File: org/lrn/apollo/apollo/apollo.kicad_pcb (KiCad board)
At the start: 2 copper layers, 28 parts, among them J1 Conn_01x01_Male, J2 Conn_01x01_Male, J3 Conn_01x01_Male, J4 Conn_01x01_Male, Q1 PN2222A, Q2 PN2222A, Q3 PN2222A, Q4 PN2222A, U1 74HC595, U2 5461AS-1

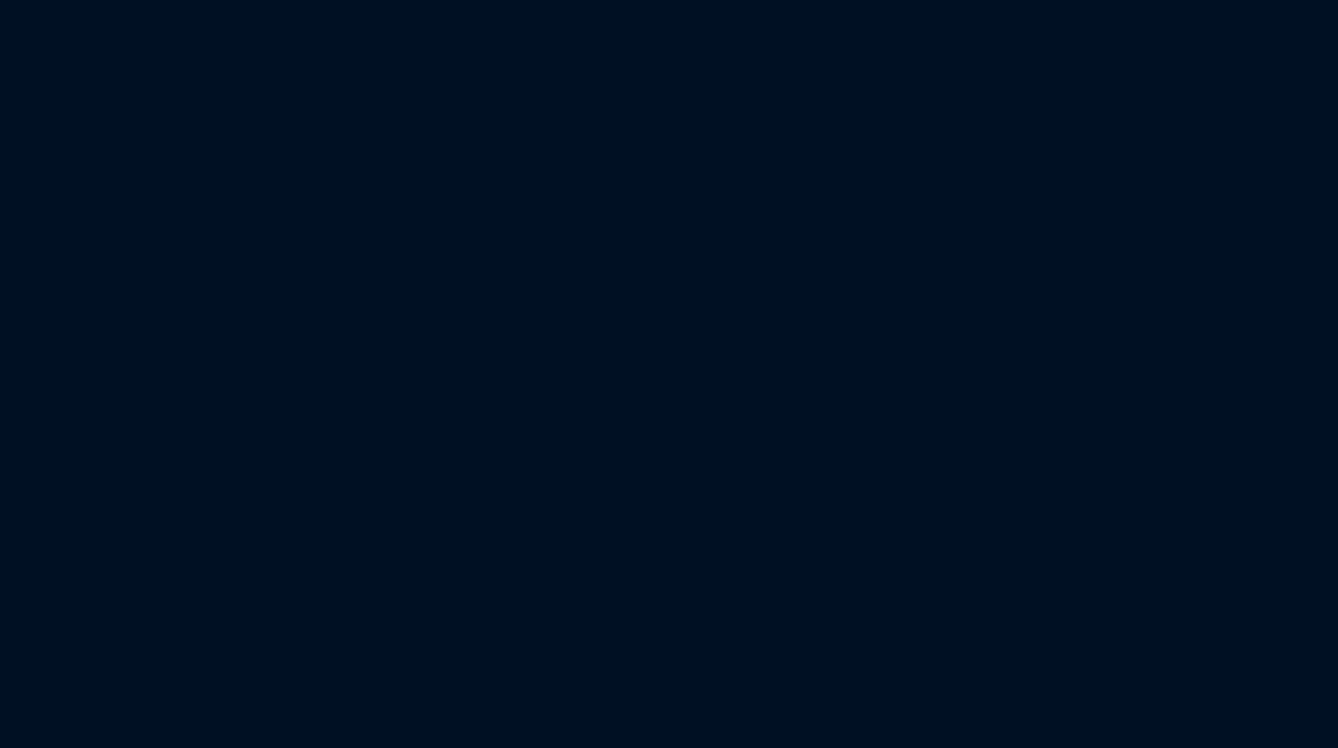
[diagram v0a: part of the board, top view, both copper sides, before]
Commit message: apollo: schematic for keyb shift register
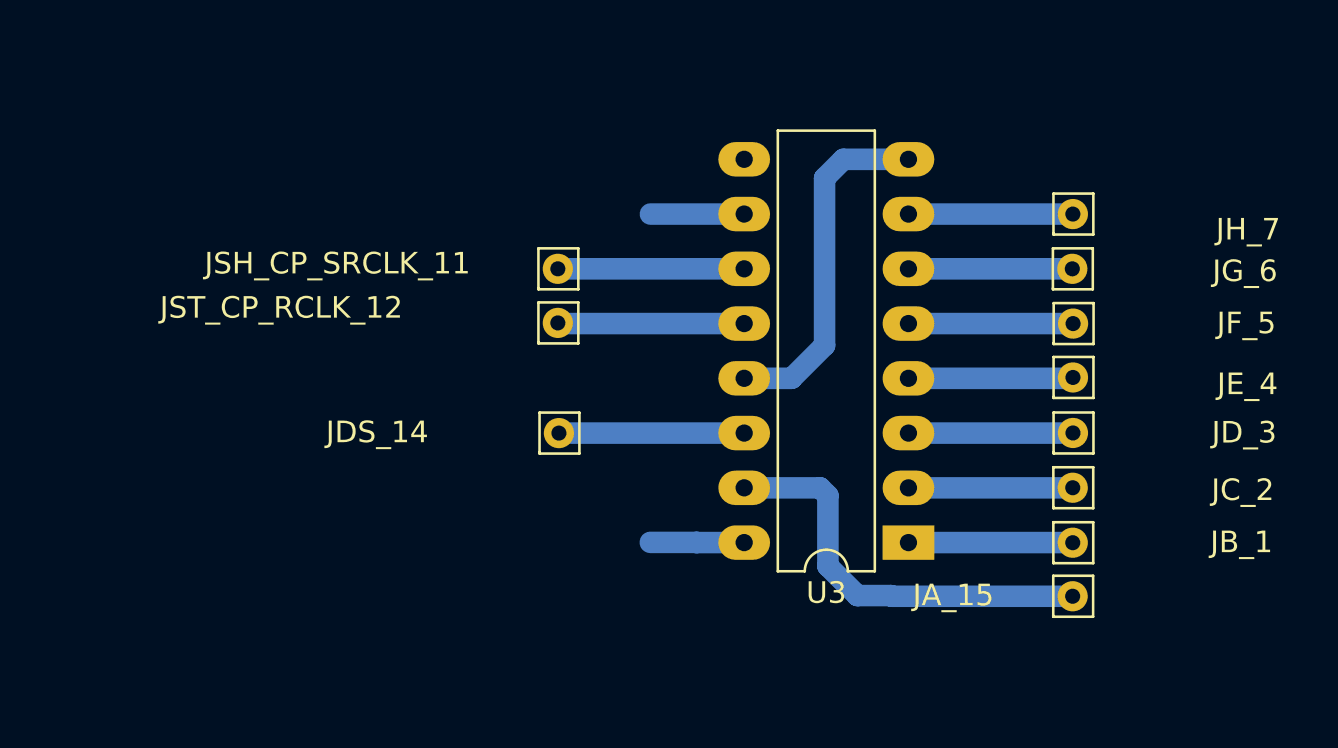
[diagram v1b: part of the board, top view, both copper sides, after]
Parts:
- added JA_15: Conn_01x01_Male, Connector_Pin:Pin_D0.7mm_L6.5mm_W1.8mm_FlatFork, F.Cu at (153.2, 95.3)
- added JB_1: Conn_01x01_Male, Connector_Pin:Pin_D0.7mm_L6.5mm_W1.8mm_FlatFork, F.Cu at (153.2, 92.8)
- added JC_2: Conn_01x01_Male, Connector_Pin:Pin_D0.7mm_L6.5mm_W1.8mm_FlatFork, F.Cu at (153.2, 90.3)
- added JDS_14: Conn_01x01_Male, Connector_Pin:Pin_D0.7mm_L6.5mm_W1.8mm_FlatFork, F.Cu at (129.4, 87.7)
- added JD_3: Conn_01x01_Male, Connector_Pin:Pin_D0.7mm_L6.5mm_W1.8mm_FlatFork, F.Cu at (153.2, 87.7)
- added JE_4: Conn_01x01_Male, Connector_Pin:Pin_D0.7mm_L6.5mm_W1.8mm_FlatFork, F.Cu at (153.2, 85.2)
- added JF_5: Conn_01x01_Male, Connector_Pin:Pin_D0.7mm_L6.5mm_W1.8mm_FlatFork, F.Cu at (153.2, 82.7)
- added JG_6: Conn_01x01_Male, Connector_Pin:Pin_D0.7mm_L6.5mm_W1.8mm_FlatFork, F.Cu at (153.2, 80.1)
- added JH_7: Conn_01x01_Male, Connector_Pin:Pin_D0.7mm_L6.5mm_W1.8mm_FlatFork, F.Cu at (153.2, 77.6)
- added JSH_CP_SRCLK_11: Conn_01x01_Male, Connector_Pin:Pin_D0.7mm_L6.5mm_W1.8mm_FlatFork, F.Cu at (129.3, 80.1)
- added JST_CP_RCLK_12: Conn_01x01_Male, Connector_Pin:Pin_D0.7mm_L6.5mm_W1.8mm_FlatFork, F.Cu at (129.3, 82.6)
- added U3: 74HC595, Package_DIP:DIP-16_W7.62mm_LongPads, F.Cu at (145.6, 92.8)
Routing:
- net Net-(JA_15-Pad1): track 0.00 -> 19.2 mm
- net GND: track 143.5 -> 159.8 mm
- net VCC: track 27.1 -> 36.1 mm
- net Net-(JST_CP_RCLK_12-Pad1): track 0.00 -> 8.66 mm
- net Net-(JSH_CP_SRCLK_11-Pad1): track 0.00 -> 8.64 mm
- net Net-(JDS_14-Pad1): track 0.00 -> 8.59 mm
- net Net-(JE_4-Pad1): track 0.00 -> 7.65 mm
- net Net-(JF_5-Pad1): track 0.00 -> 7.64 mm
- net Net-(JD_3-Pad1): track 0.00 -> 7.63 mm
- net Net-(JH_7-Pad1): track 0.00 -> 7.63 mm
- net Net-(JB_1-Pad1): track 0.00 -> 7.62 mm
- net Net-(JC_2-Pad1): track 0.00 -> 7.62 mm
- net Net-(JG_6-Pad1): track 0.00 -> 7.60 mm

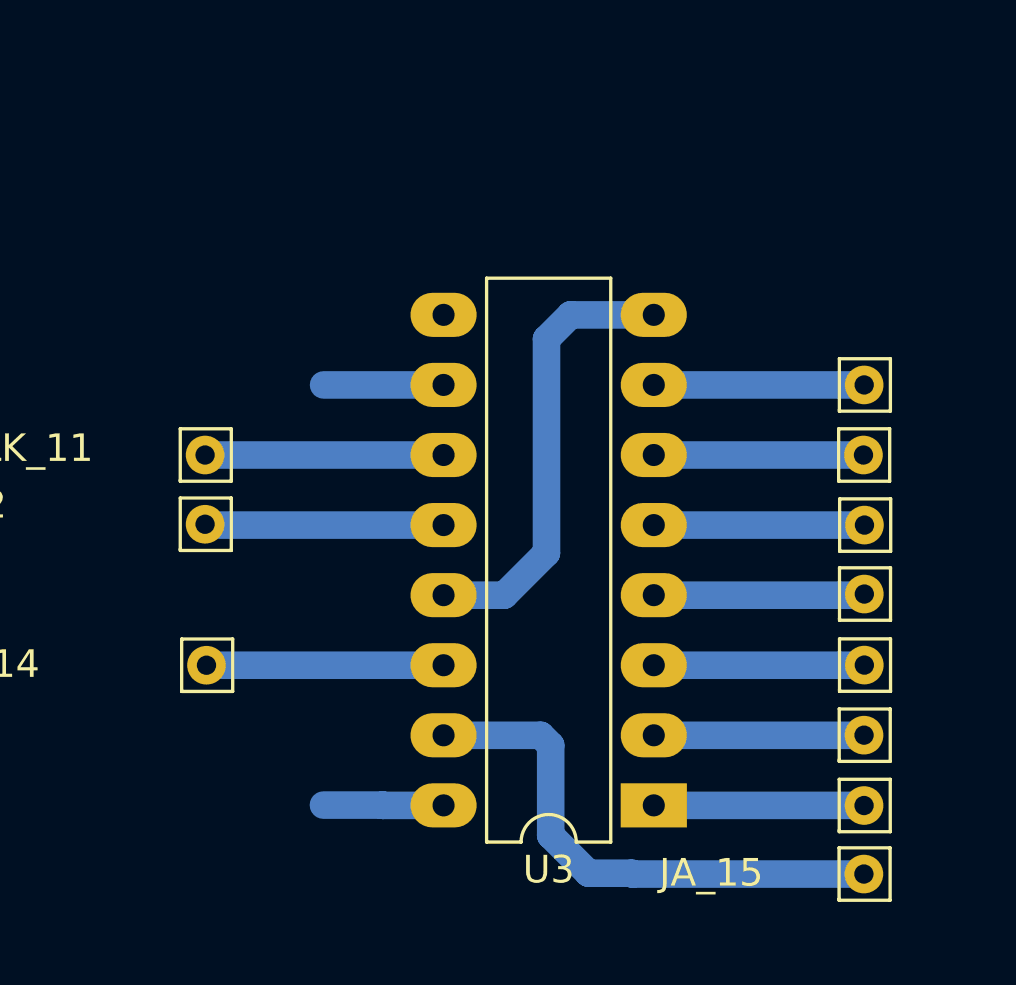
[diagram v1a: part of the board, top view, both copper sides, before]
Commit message: apollo: keyb driver: additional track-vias
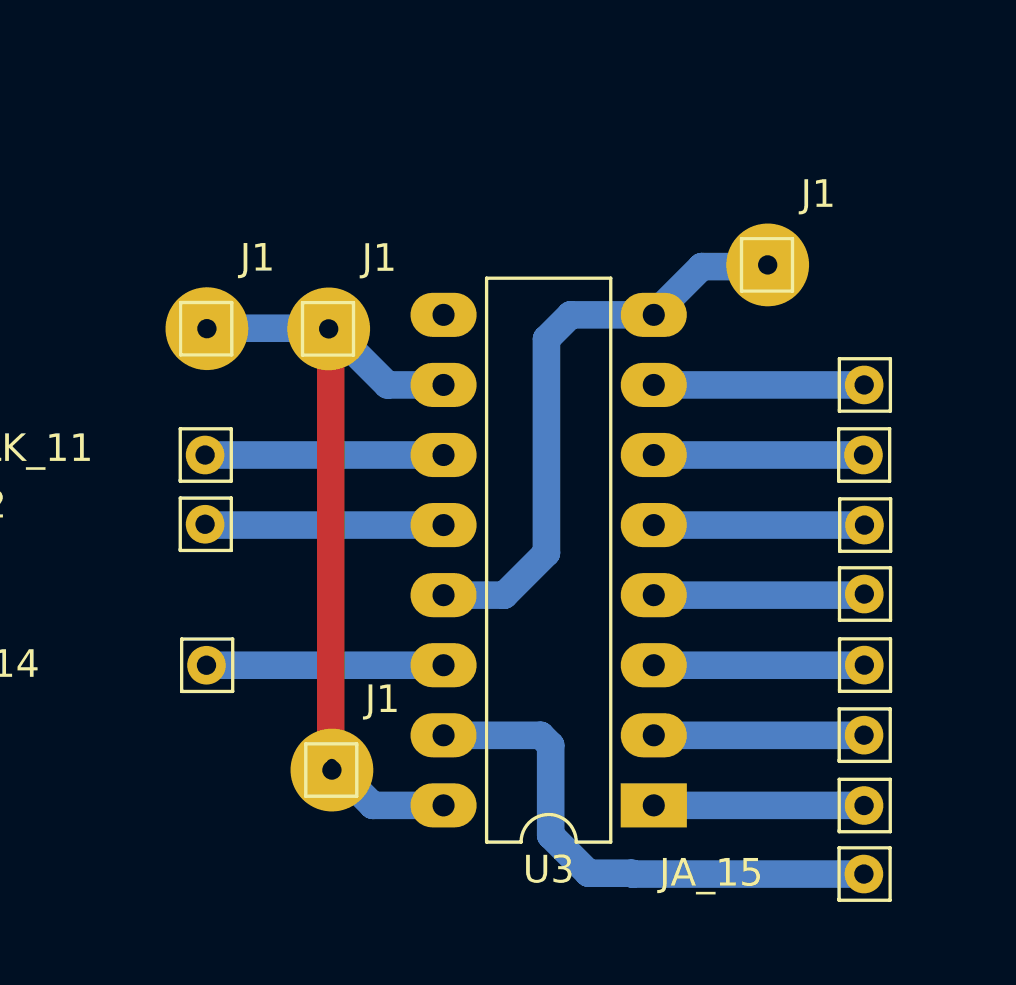
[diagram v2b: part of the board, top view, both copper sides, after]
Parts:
- added J1: Conn_01x01_Male, Connector_Pin:Pin_D0.7mm_L6.5mm_W1.8mm_FlatFork, F.Cu at (133.8, 75.6)
- added J1: Conn_01x01_Male, Connector_Pin:Pin_D0.7mm_L6.5mm_W1.8mm_FlatFork, F.Cu at (133.9, 91.5)
- added J1: Conn_01x01_Male, Connector_Pin:Pin_D0.7mm_L6.5mm_W1.8mm_FlatFork, F.Cu at (129.4, 75.5)
- added J1: Conn_01x01_Male, Connector_Pin:Pin_D0.7mm_L6.5mm_W1.8mm_FlatFork, F.Cu at (149.7, 73.2)
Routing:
- net VCC: track 36.1 -> 56.8 mm, vias 0 -> 2
- net GND: track 159.8 -> 164.7 mm

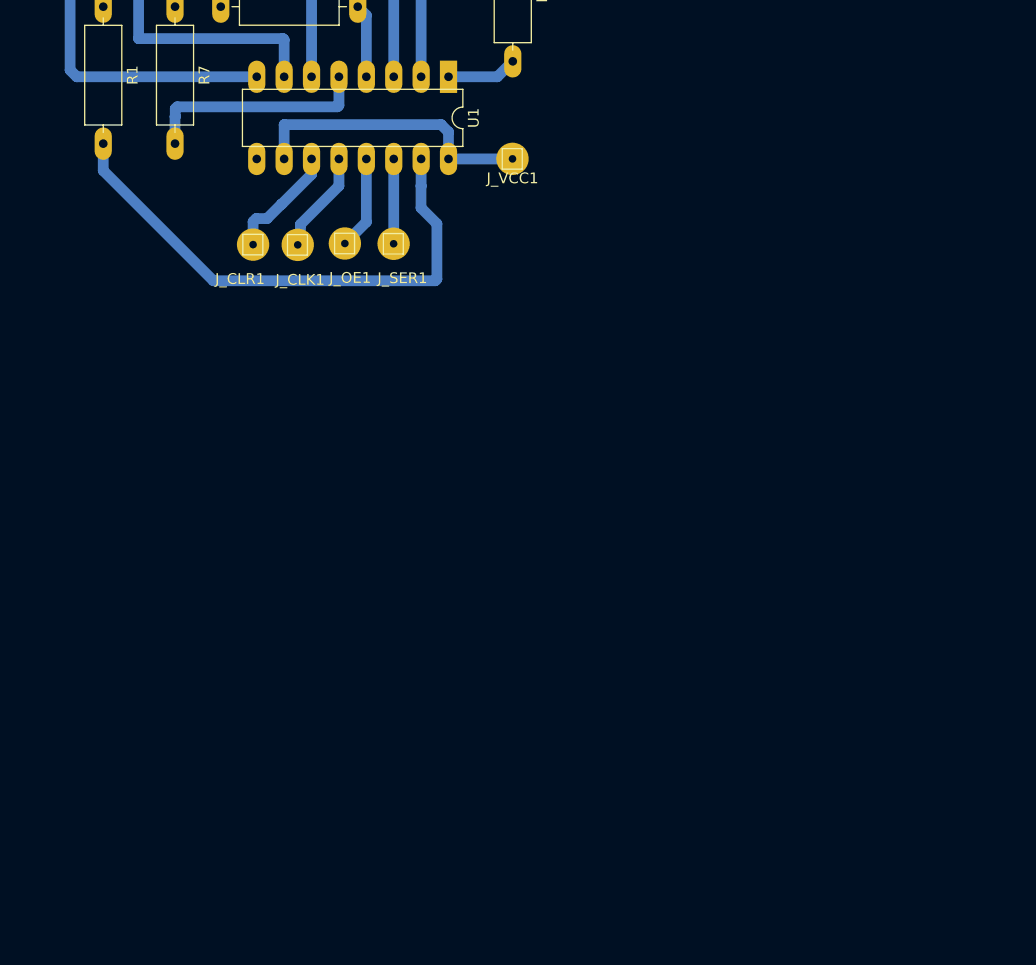
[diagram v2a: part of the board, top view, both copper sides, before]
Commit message: apollo: display works w/o timing
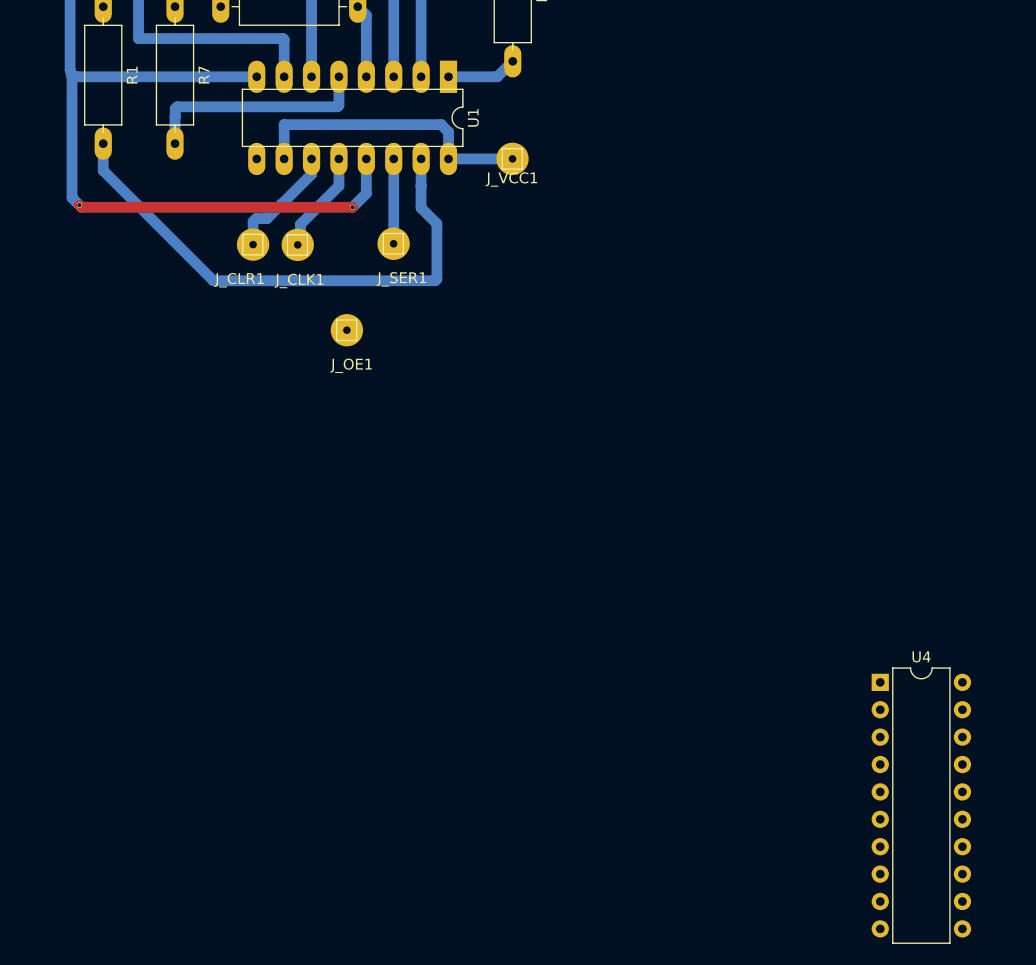
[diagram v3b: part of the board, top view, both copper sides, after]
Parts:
- added U4: ATtiny2313A-PU, Package_DIP:DIP-20_W7.62mm, F.Cu at (99.5, 147.7)
- moved J_OE1 8.04 mm to (50.0, 115.0)
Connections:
- J1 pad 1: (no net) -> Net-(J1-Pad1) (x4)
- U1 pad 13: Net-(J_OE1-Pad1) -> GND
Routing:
- net GND: track 164.7 -> 207.5 mm, vias 0 -> 2
- net Net-(J_OE1-Pad1): track 8.66 -> 0.00 mm

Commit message: apollo: update schematic (draft)
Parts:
- removed the J1 at (133.9, 91.5)
- removed the J1 at (129.4, 75.5)
- removed the J1 at (149.7, 73.2)
- removed J_OE1: Conn_01x01_Male, Connector_Pin:Pin_D0.7mm_L6.5mm_W1.8mm_FlatFork
- added J1: Conn_01x01_Male, Connector_Pin:Pin_D0.7mm_L6.5mm_W1.8mm_FlatFork, F.Cu at (197.1, 143.6)
- added J1: Conn_01x01_Male, Connector_Pin:Pin_D0.7mm_L6.5mm_W1.8mm_FlatFork, F.Cu at (192.6, 127.6)
- added J1: Conn_01x01_Male, Connector_Pin:Pin_D0.7mm_L6.5mm_W1.8mm_FlatFork, F.Cu at (212.9, 125.3)
- U4: value ATtiny2313A-PU -> ATmega168P-20PU; footprint Package_DIP:DIP-20_W7.62mm -> Package_DIP:DIP-28_W7.62mm
- moved U4 99.3 mm to (89.1, 48.9), turned to 90 degrees
- moved JF_5 81.9 mm to (216.4, 134.7)
- moved R5 81.9 mm to (128.6, 129.4)
- moved J1 81.9 mm to (197.0, 127.6)
- moved J2 81.9 mm to (88.4, 76.0)
- moved J3 81.9 mm to (100.4, 76.0)
- moved J4 81.9 mm to (113.2, 76.0)
- moved JB_1 81.9 mm to (216.4, 144.9)
- moved JD_3 81.9 mm to (216.4, 139.8)
- moved JE_4 81.9 mm to (216.4, 137.2)
- moved JH_7 81.9 mm to (216.4, 129.6)
- moved JST_CP_RCLK_12 81.9 mm to (192.5, 134.7)
- moved J_CLK1 81.9 mm to (108.6, 159.1)
- moved J_GND1 81.9 mm to (87.6, 84.0)
- moved J_SER1 81.9 mm to (117.5, 159.0)
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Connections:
- U4 pad 15: Net-(U4-Pad15) -> Net-(J1-Pad1)
- U4 pad 8: Net-(U4-Pad8) -> Net-(U4-Pad22)
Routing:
- net Net-(J_CLK1-Pad1): track 9.55 -> 295.1 mm, vias 0 -> 3
- net Net-(J_CLR1-Pad1): track 10.8 -> 277.0 mm, vias 0 -> 1
- net Net-(J_SER1-Pad1): track 7.87 -> 228.9 mm, vias 0 -> 2
- net Net-(J3-Pad1): track 6.75 -> 99.7 mm, vias 0 -> 2
- net Net-(J4-Pad1): track 6.02 -> 89.7 mm, vias 0 -> 2
- net Net-(J2-Pad1): track 6.42 -> 87.6 mm
- net Net-(J1-Pad1): track 5.94 -> 50.3 mm

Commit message: apollo: schematic updated
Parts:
- removed the J1 at (197.1, 143.6)
- removed the J1 at (192.6, 127.6)
- removed the J1 at (212.9, 125.3)
- added J1: Conn_01x01_Male, Connector_Pin:Pin_D0.7mm_L6.5mm_W1.8mm_FlatFork, F.Cu at (-12.7, 148.3)
- added J1: Conn_01x01_Male, Connector_Pin:Pin_D0.7mm_L6.5mm_W1.8mm_FlatFork, F.Cu at (-17.2, 132.3)
- added J1: Conn_01x01_Male, Connector_Pin:Pin_D0.7mm_L6.5mm_W1.8mm_FlatFork, F.Cu at (3.12, 130.0)
- added J_MISO_1: Conn_01x01_Male, Connector_Pin:Pin_D0.7mm_L6.5mm_W1.8mm_FlatFork, F.Cu at (134.1, 66.4)
- added J_MOSI_1: Conn_01x01_Male, Connector_Pin:Pin_D0.7mm_L6.5mm_W1.8mm_FlatFork, F.Cu at (134.1, 63.9)
- added J_SCK_1: Conn_01x01_Male, Connector_Pin:Pin_D0.7mm_L6.5mm_W1.8mm_FlatFork, F.Cu at (134.1, 69.0)
- moved JB_1 209.8 mm to (6.61, 149.6)
- moved JC_2 209.8 mm to (6.61, 147.1)
- moved JDS_14 209.8 mm to (-17.2, 144.5)
- moved JG_6 209.8 mm to (6.59, 136.9)
- moved JH_7 209.8 mm to (6.62, 134.4)
- moved U3 209.8 mm to (-1.01, 149.6)
- moved J1 209.8 mm to (-12.8, 132.3)
- moved JA_15 209.8 mm to (6.61, 152.1)
- moved JD_3 209.8 mm to (6.62, 144.5)
- moved JE_4 209.8 mm to (6.62, 142.0)
- moved JF_5 209.8 mm to (6.63, 139.5)
- moved JSH_CP_SRCLK_11 209.8 mm to (-17.3, 136.9)
- moved JST_CP_RCLK_12 209.8 mm to (-17.3, 139.4)
- moved U4 71.0 mm to (145.6, 91.8), turned to 180 degrees
- moved Q1 4.39 mm to (125.2, 90.0), turned to 270 degrees
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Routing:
- net Net-(J_CLK1-Pad1): track 295.1 -> 121.2 mm, vias 3 -> 1
- net Net-(J_CLR1-Pad1): track 277.0 -> 145.1 mm
- net Net-(J_SER1-Pad1): track 228.9 -> 101.0 mm, vias 2 -> 1
- net Net-(J4-Pad1): track 89.7 -> 27.6 mm, vias 2 -> 0
- net Net-(J3-Pad1): track 99.7 -> 42.9 mm, vias 2 -> 0
- net Net-(J2-Pad1): track 87.6 -> 57.6 mm
- net Net-(J1-Pad1): track 50.3 -> 30.0 mm
- net GND: track 207.5 -> 191.9 mm
- net Net-(Q4-Pad3): track 13.7 -> 5.40 mm
- net Net-(Q2-Pad3): track 10.7 -> 17.8 mm
- net Net-(Q3-Pad3): track 7.94 -> 12.8 mm
- net Net-(Q1-Pad3): track 83.4 -> 87.7 mm
- net Net-(J_MISO_1-Pad1): track 0.00 -> 3.91 mm
- net Net-(J_SCK_1-Pad1): track 0.00 -> 3.90 mm
- net Net-(J_MOSI_1-Pad1): track 0.00 -> 3.90 mm
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
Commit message: apollo: schematic optimization layout
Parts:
- removed the J1 at (-12.7, 148.3)
- removed the J1 at (-17.2, 132.3)
- removed the J1 at (3.12, 130.0)
- added J1: Conn_01x01_Male, Connector_Pin:Pin_D0.7mm_L6.5mm_W1.8mm_FlatFork, F.Cu at (95.1, 122.2)
- added J1: Conn_01x01_Male, Connector_Pin:Pin_D0.7mm_L6.5mm_W1.8mm_FlatFork, F.Cu at (90.6, 106.2)
- added J1: Conn_01x01_Male, Connector_Pin:Pin_D0.7mm_L6.5mm_W1.8mm_FlatFork, F.Cu at (110.9, 103.9)
- moved J_GND1 135.8 mm to (217.1, 45.5)
- moved R4 110.9 mm to (219.5, 95.9)
- moved U2 110.9 mm to (216.9, 65.4)
- moved U3 110.9 mm to (106.8, 123.5)
- moved J1 110.9 mm to (95.0, 106.2)
- moved JA_15 110.9 mm to (114.4, 126.0)
- moved JB_1 110.9 mm to (114.4, 123.5)
- moved JC_2 110.9 mm to (114.4, 121.0)
- moved JDS_14 110.9 mm to (90.6, 118.4)
- moved JD_3 110.9 mm to (114.4, 118.4)
- moved JE_4 110.9 mm to (114.4, 115.8)
- moved JF_5 110.9 mm to (114.4, 113.4)
- moved JG_6 110.9 mm to (114.4, 110.8)
- moved JH_7 110.9 mm to (114.4, 108.3)
- moved JSH_CP_SRCLK_11 110.9 mm to (90.5, 110.8)
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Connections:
- U4 pad 15: Net-(J1-Pad1) -> Net-(U4-Pad15)
- U4 pad 16: Net-(U4-Pad16) -> Net-(J_CLK1-Pad1)
- U4 pad 22: Net-(U4-Pad22) -> GND
- U4 pad 23: Net-(J4-Pad1) -> Net-(J2-Pad1)
- U4 pad 25: Net-(J2-Pad1) -> Net-(J4-Pad1)
- U4 pad 26: Net-(J_SER1-Pad1) -> Net-(J1-Pad1)
- U4 pad 27: Net-(J_CLR1-Pad1) -> Net-(J_SER1-Pad1)
- U4 pad 28: Net-(J_CLK1-Pad1) -> Net-(J_CLR1-Pad1)
- U4 pad 7: Net-(U4-Pad7) -> VCC
- U4 pad 8: Net-(U4-Pad22) -> GND
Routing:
- net GND: track 191.9 -> 239.8 mm
- net Net-(J_CLK1-Pad1): track 121.2 -> 142.1 mm, vias 1 -> 2
- net Net-(J_SER1-Pad1): track 101.0 -> 120.4 mm, vias 1 -> 0
- net Net-(J2-Pad1): track 57.6 -> 41.2 mm
- net Net-(R1-Pad2): track 49.5 -> 37.0 mm, vias 0 -> 2
- net Net-(J3-Pad1): track 42.9 -> 32.2 mm
- net Net-(J_CLR1-Pad1): track 145.1 -> 155.8 mm, vias 1 -> 0
- net Net-(Q1-Pad3): track 87.7 -> 84.3 mm
- net Net-(J_MISO_1-Pad1): track 3.91 -> 6.68 mm
- net Net-(J_SCK_1-Pad1): track 3.90 -> 6.67 mm
- net Net-(J_MOSI_1-Pad1): track 3.90 -> 6.67 mm
- net Net-(J4-Pad1): track 27.6 -> 25.1 mm
- net Net-(J1-Pad1): track 30.0 -> 32.4 mm
- net Net-(Q4-Pad2): track 7.43 -> 5.04 mm
- net Net-(Q3-Pad3): track 12.8 -> 14.9 mm
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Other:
- net class Default: clearance 0.2 -> 0.8
- rule trace_clearance: 0.2 -> 0.8

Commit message: apollo: pcm updated
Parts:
- moved J2 27.4 mm to (221.8, 48.0)
- moved J_GND1 22.2 mm to (195.0, 48.0)
- moved J3 21.5 mm to (227.7, 48.0)
- moved J4 16.0 mm to (233.5, 48.0)
- moved J1 11.6 mm to (239.3, 48.0)
- moved J_MISO_1 1.04 mm to (209.2, 44.4)
- moved J_MOSI_1 1.04 mm to (206.6, 44.4)
- moved J_SCK_1 1.04 mm to (211.7, 44.4)
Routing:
- net Net-(J2-Pad1): track 41.2 -> 29.7 mm
- net Net-(J1-Pad1): track 32.4 -> 23.0 mm
- net Net-(J3-Pad1): track 32.2 -> 26.1 mm
- net Net-(J_CLR1-Pad1): track 155.8 -> 160.7 mm
- net Net-(J4-Pad1): track 25.1 -> 20.7 mm
- net Net-(J_SER1-Pad1): track 120.4 -> 124.7 mm
- net Net-(J_CLK1-Pad1): track 142.1 -> 145.5 mm
- net GND: track 239.8 -> 241.8 mm
- net Net-(J_SCK_1-Pad1): track 6.67 -> 5.63 mm
- net Net-(J_MOSI_1-Pad1): track 6.67 -> 5.63 mm
- net Net-(J_MISO_1-Pad1): track 6.68 -> 5.64 mm
